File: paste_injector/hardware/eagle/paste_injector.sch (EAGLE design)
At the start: 16 parts, among them J1 USB, Q1 CSTCR6M00G53Z, U1 ATMEGA328TQFP32, U2 ULN2003AD

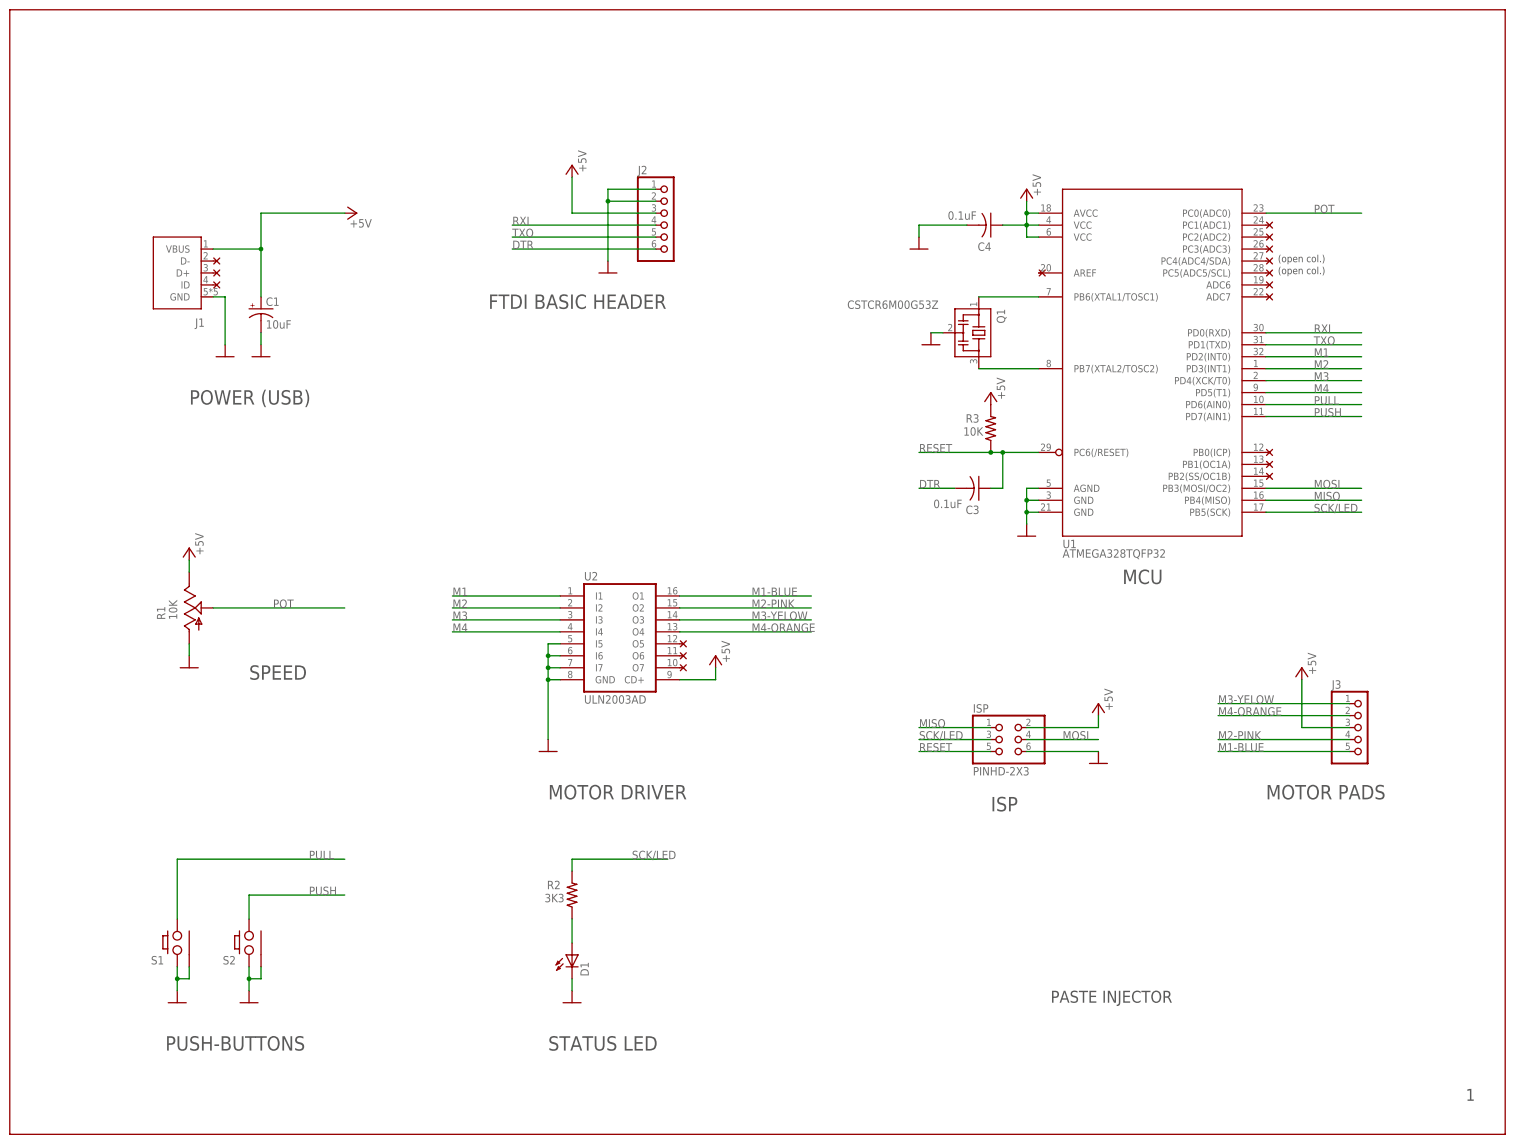
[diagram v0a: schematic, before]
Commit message: added oled
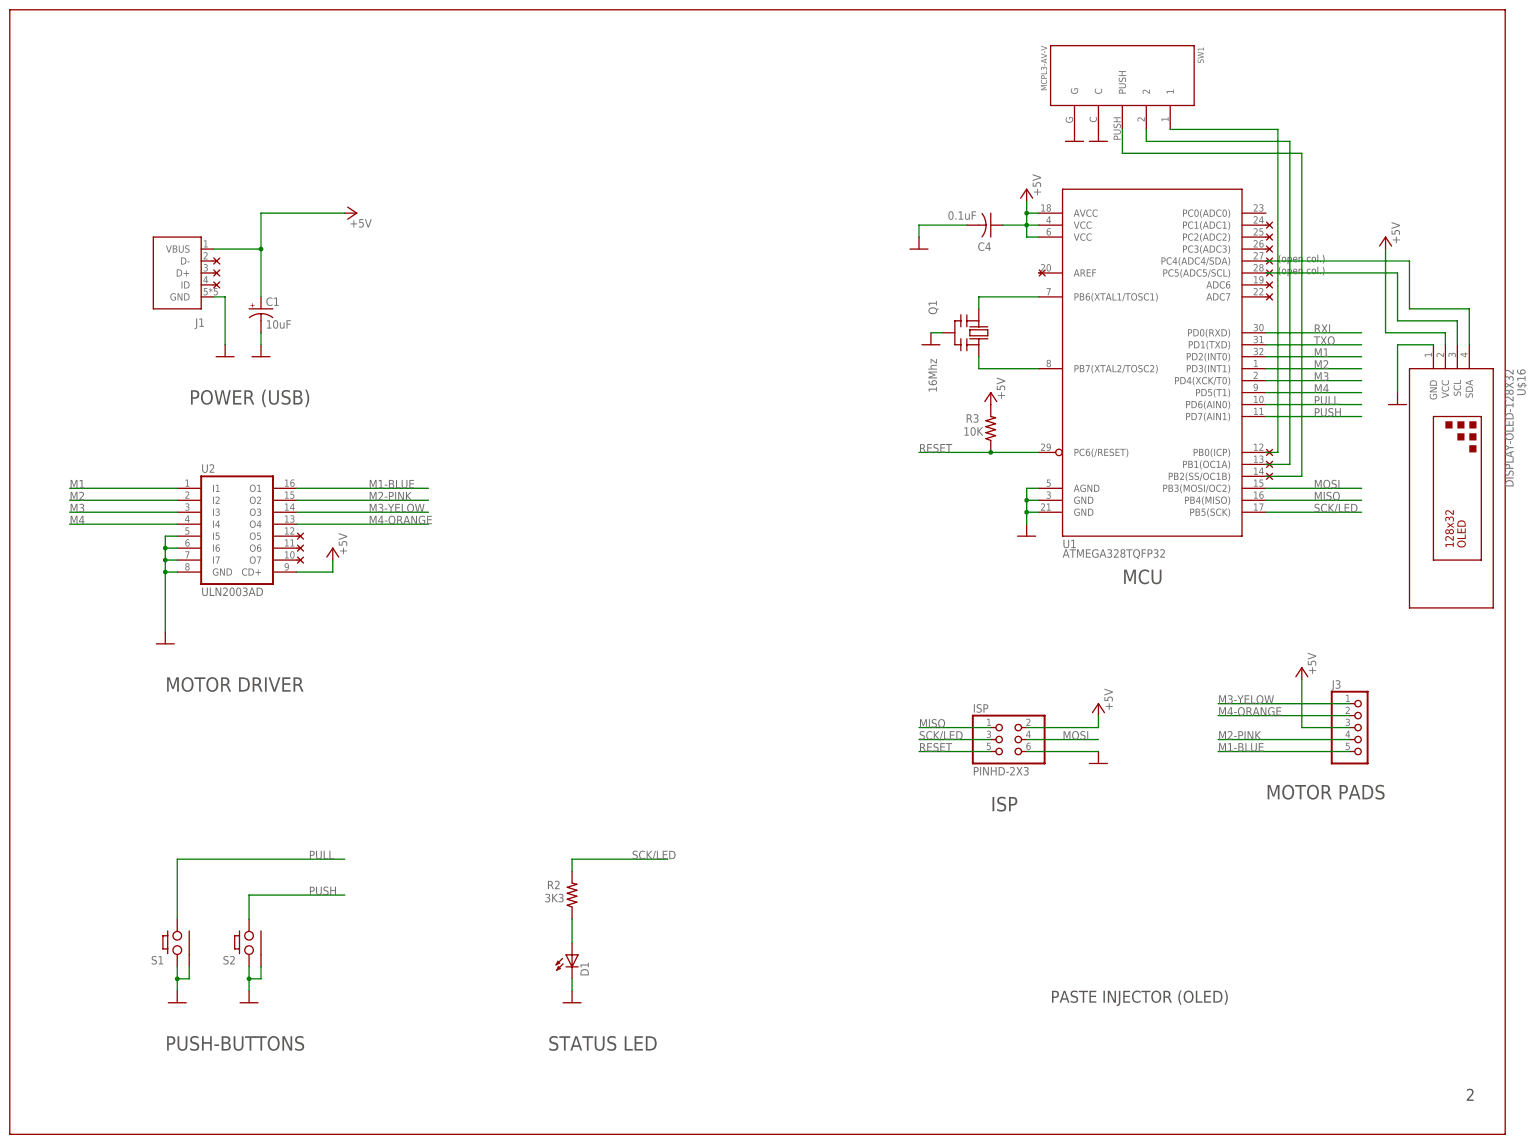
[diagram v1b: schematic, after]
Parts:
- removed C3: 0.1uF, paste_injector:CAP-C0603
- removed J2: (no value), paste_injector:PINHD-1X6
- removed R1: 10K, paste_injector:TRIMPOTCA9V
- added SW1: MCPL3-AV-V, lbrzak:MCPL3-AV-V
- added U$16: DISPLAY-OLED-128X32, diy-modules:DISPLAY-OLED-128X32
- Q1: value CSTCR6M00G53Z -> 16Mhz; device paste_injector:CSTCR6M00G53Z -> adafruit:CERMOSCILL-CSTCRG
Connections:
- removed net DTR: C3.2, J2.6
- removed net POT: R1.C, U1.PC0(ADC0)
- new net N$3: U$16.SDA, U1.PC4(ADC4/SDA)
- new net N$4: U$16.SCL, U1.PC5(ADC5/SCL)
- new net N$5: SW1.1, U1.PB0(ICP)
- new net N$6: SW1.2, U1.PB1(OC1A)
- new net N$8: SW1.PUSH, U1.PB2(SS/OC1B)
- net +5V: now also U$16.VCC; no longer J2.3, R1.CW
- net GND: now also Q1.GND, SW1.C, SW1.G, U$16.GND; no longer J2.1, J2.2, Q1.2, R1.CCW
- net N$2: now also Q1.IN; no longer Q1.1
- net N$7: now also Q1.OUT; no longer Q1.3
- net RESET: no longer C3.1
- net RXI: no longer J2.4
- net TXO: no longer J2.5
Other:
- note added: "2"
- note added: "PASTE INJECTOR (OLED)"
- note removed: "+5V"
- note removed: "1"
- note removed: "CTS"
- note removed: "DTR"
- note removed: "FTDI BASIC HEADER"
- note removed: "GND"
- note removed: "PASTE INJECTOR"
- note removed: "RXI"
- note removed: "SPEED"
- note removed: "TXO"
- moved on the sheet: U2

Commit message: make board
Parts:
- removed S1, S2: PUSH_BUTTON, paste_injector:PUSH_BUTTON
- added P-BUTT.: (no value), jumper:JP2E
- renumbered U$16 to U3
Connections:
- net GND: now also P-BUTT..3; no longer S1.1, S1.GND, S2.1, S2.GND
- net PULL: now also P-BUTT..1; no longer S1.2
- net PUSH: now also P-BUTT..2; no longer S2.2
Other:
- note added: "PUSH-BUTTONS JUMPER contact to GND."
- note removed: "(open col.)"
- note removed: "PUSH-BUTTONS"
